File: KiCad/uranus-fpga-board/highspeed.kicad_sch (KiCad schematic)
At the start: 8 parts, among them J1 1040100018, J2 TYPE-C-31-M-12, J4 ASP-134486-01, U6 FT232HL-REEL, U7 93LC56BT, U8 USBLC6-2SC6, U9 W25Q128JVSIQ, Y2 3225-12-20-10-10/4B

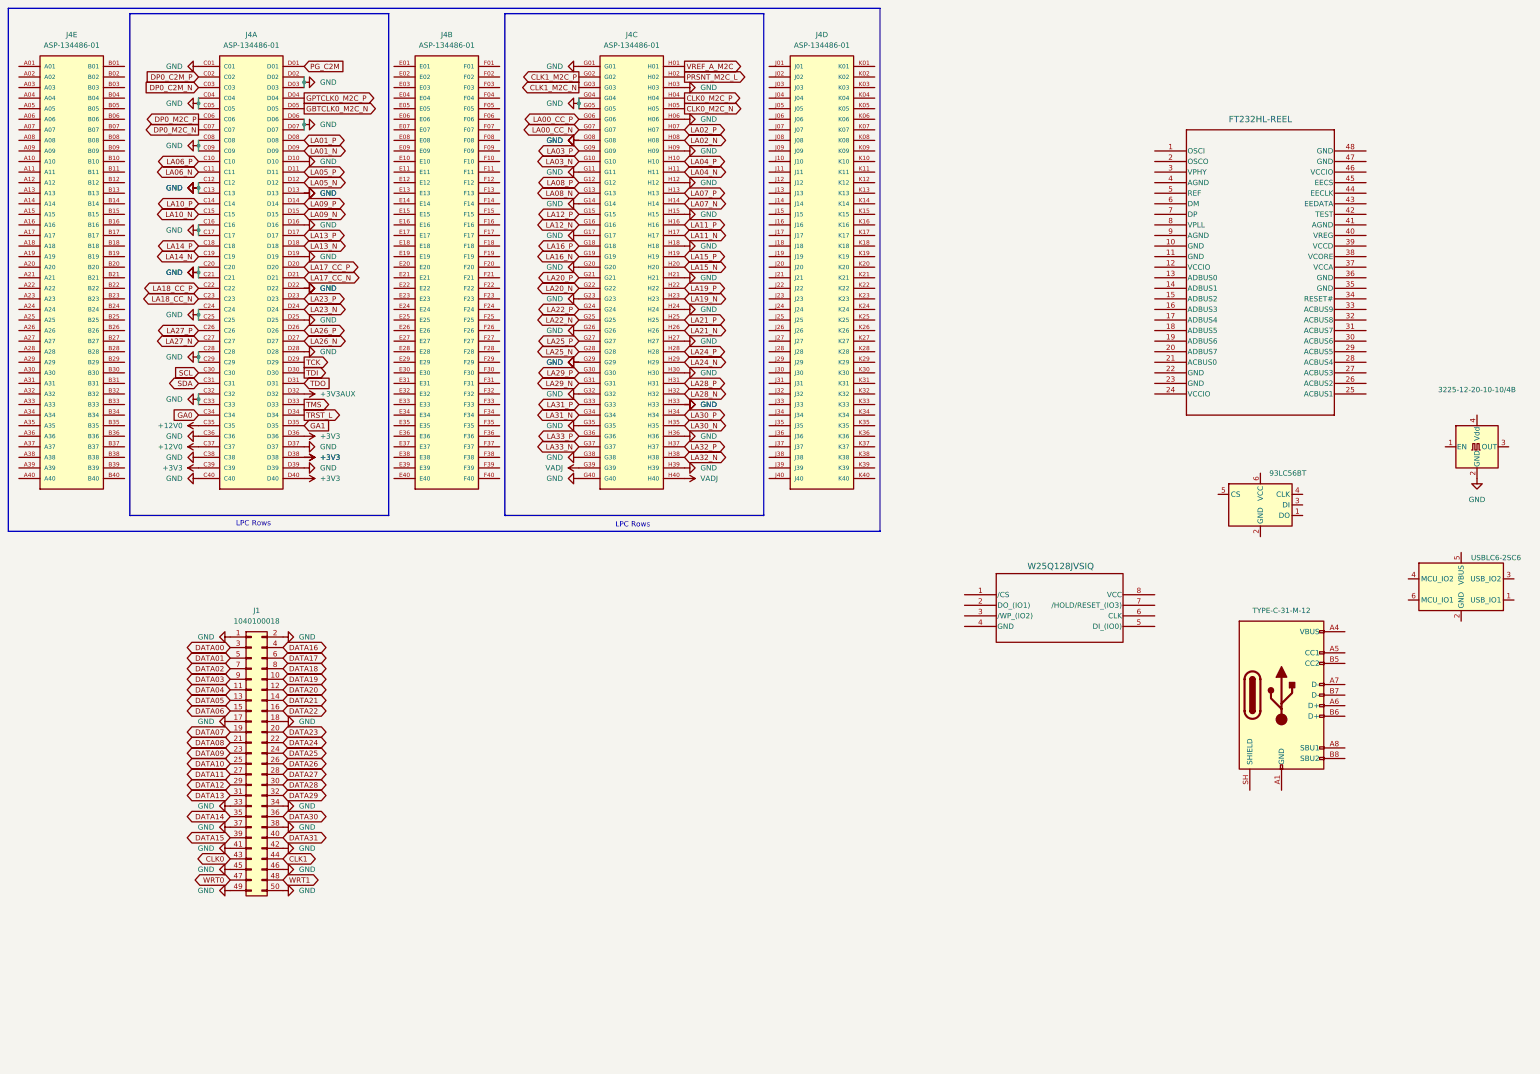
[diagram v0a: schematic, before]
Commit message: New journal, moved BOMS into a new directory
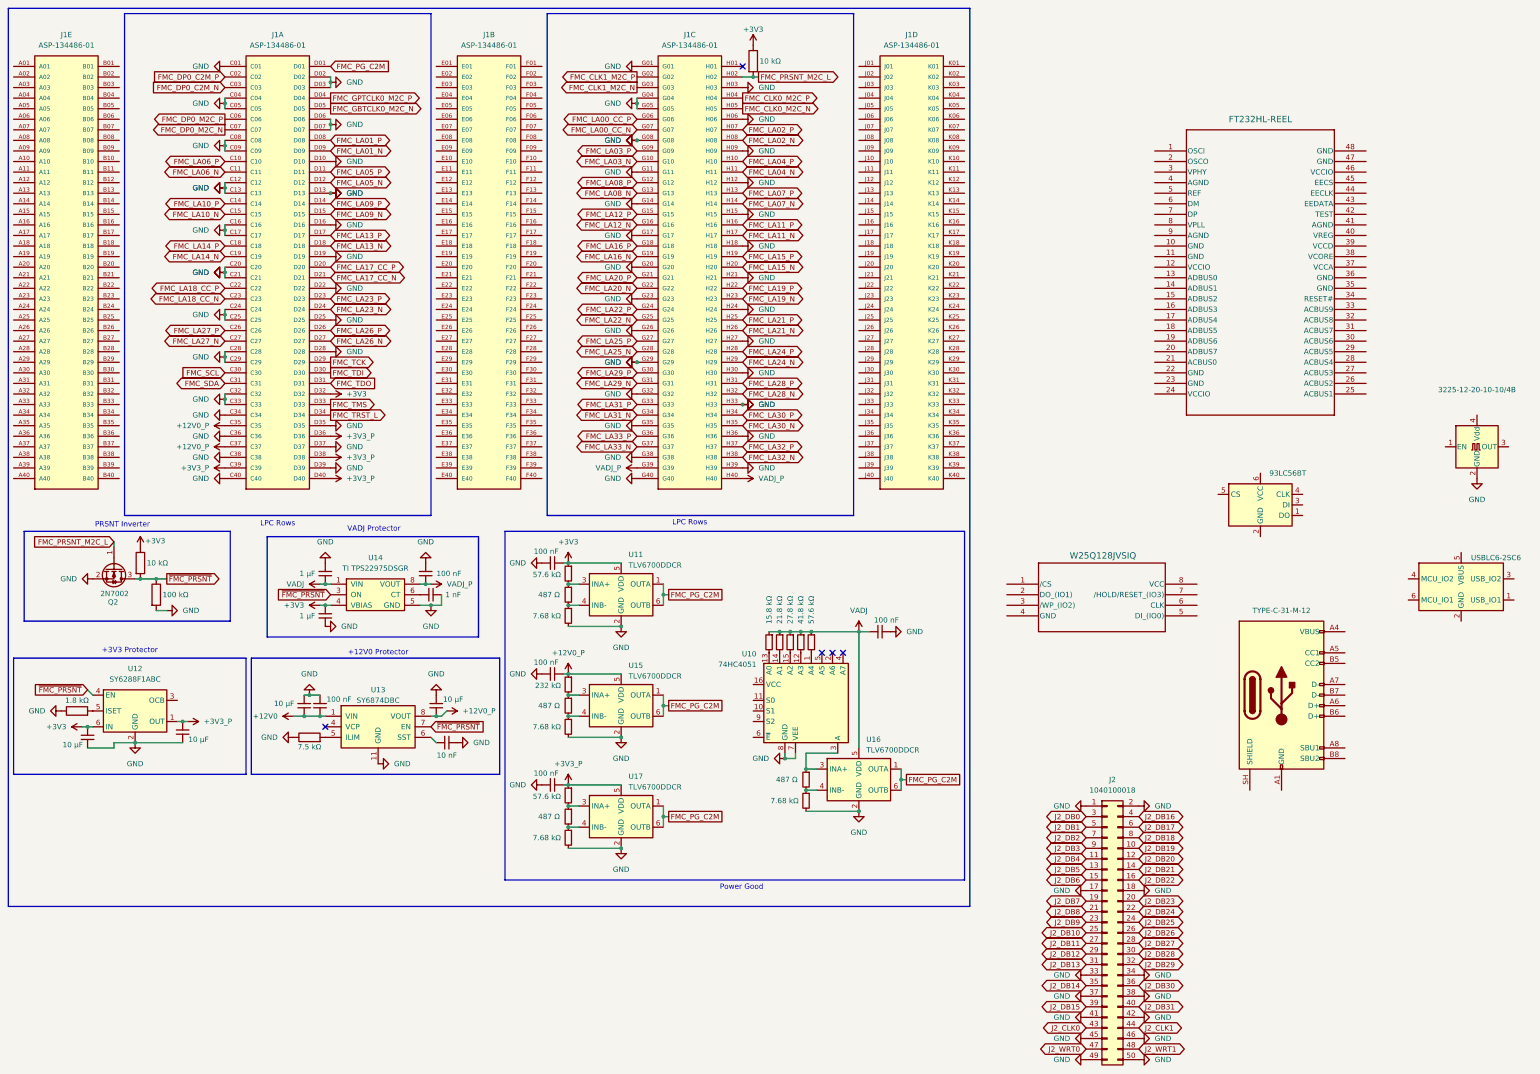
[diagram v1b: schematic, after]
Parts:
- added C68: 1 nF, symbol Device:C_Small
- added C69: 10 nF, symbol Device:C_Small
- added C70, C71, C75, C76: 10 μF, symbol Device:C_Small
- added C72, C77: 1 μF, symbol Device:C_Small
- added C73, C74, C78, C79, C80, C81: 100 nF, symbol Device:C_Small
- added Q2: 2N7002, Package_TO_SOT_SMD:SOT-23, symbol Transistor_FET:2N7002
- added R13, R24, R31: 57.6 kΩ, symbol Device:R_Small
- added R14, R22, R25, R32: 487 Ω, symbol Device:R_Small
- added R15, R16: 10 kΩ, symbol Device:R
- added R17: 7.5 kΩ, symbol Device:R
- added R18: 1.8 kΩ, symbol Device:R
- added R19: 100 kΩ, symbol Device:R
- added R20, R23, R26, R33: 7.68 kΩ, symbol Device:R_Small
- added R21: 232 kΩ, symbol Device:R_Small
- added R27: 41.8 kΩ, symbol Device:R_Small
- added R28: 27.8 kΩ, symbol Device:R_Small
- added R29: 21.8 kΩ, symbol Device:R_Small
- added R30: 15.8 kΩ, symbol Device:R_Small
- added U10: 74HC4051, Package_SO:SOIC-16_3.9x9.9mm_P1.27mm, symbol 74xx:74HC4051
- added U11, U15, U16, U17: TLV6700DDCR, Package_TO_SOT_SMD:SOT-23-6, symbol Sensor_Touch:AT42QT1011-TSHR
- added U12: SY6288F1ABC, Package_TO_SOT_SMD:SOT-23-6, symbol Power_Management:AP2171W
- added U13: SY6874DBC, Package_DFN_QFN:DFN-10-1EP_3x3mm_P0.5mm_EP1.75x2.7mm, symbol Connector_Generic:Conn_02x05_Counter_Clockwise
- added U14: TI TPS22975DSGR, Package_SON:Texas_DSG0008A_WSON-8-1EP_2x2mm_P0.5mm_EP0.9x1.6mm, symbol Connector_Generic:Conn_02x04_Counter_Clockwise
- renumbered J4 to J1, J1 to J2, J2 to J3, U9 to U6, U6 to U7, U7 to U8, U8 to U9
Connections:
- net +3V3AUX is gone; now on net +3V3: J1.D32
- net GA0 is gone; now on net GND: J1.C34
- net GA1 is gone; now on net GND: J1.D35
- net +12V0: now also C74.2, C75.2, U13.1 (VIN), U13.2 (VIN), U13.3 (VIN); no longer J1.C35, J1.C37
- net +3V3: now also C70.1, C77.2, C78.2, R13.1, R15.1, R16.1, U11.5 (VDD), U12.6 (IN), U14.4 (VBIAS); no longer J1.C39, J1.D36, J1.D38, J1.D40
- net GND: now also C68.2, C69.2, C70.2, C71.2, C72.1, C73.1, C74.1, C75.1, C76.1, C77.1, C78.1, C79.1, C80.1, C81.1, Q2.2 (S), R17.1, R18.1, R19.2, R20.2, R23.2, R26.2, R33.2, U10.7 (VEE), U10.8 (GND), U11.2 (GND), U12.2 (GND), U13.11 (GND), U14.5 (GND), U15.2 (GND), U16.2 (GND), U17.2 (GND)
- net VADJ: now also C72.2, C80.2, R24.1, R27.1, R28.1, R29.1, R30.1, U14.1 (VIN), U14.2 (VIN), U16.5 (VDD); no longer J1.G39, J1.H40
- net CLK0 renamed J2_CLK0
- net CLK0_M2C_N renamed FMC_CLK0_M2C_N
- net CLK0_M2C_P renamed FMC_CLK0_M2C_P
- net CLK1 renamed J2_CLK1
- net CLK1_M2C_N renamed FMC_CLK1_M2C_N
- net CLK1_M2C_P renamed FMC_CLK1_M2C_P
- net DATA00 renamed J2_DB0
- net DATA01 renamed J2_DB1
- net DATA02 renamed J2_DB2
- net DATA03 renamed J2_DB3
- net DATA04 renamed J2_DB4
- net DATA05 renamed J2_DB5
- net DATA06 renamed J2_DB6
- net DATA07 renamed J2_DB7
- net DATA08 renamed J2_DB8
- net DATA09 renamed J2_DB9
- net DATA10 renamed J2_DB10
- net DATA11 renamed J2_DB11
- net DATA12 renamed J2_DB12
- net DATA13 renamed J2_DB13
- net DATA14 renamed J2_DB14
- net DATA15 renamed J2_DB15
- net DATA16 renamed J2_DB16
- net DATA17 renamed J2_DB17
- net DATA18 renamed J2_DB18
- net DATA19 renamed J2_DB19
- net DATA20 renamed J2_DB20
- net DATA21 renamed J2_DB21
- net DATA22 renamed J2_DB22
- net DATA23 renamed J2_DB23
- net DATA24 renamed J2_DB24
- net DATA25 renamed J2_DB25
- net DATA26 renamed J2_DB26
- net DATA27 renamed J2_DB27
- net DATA28 renamed J2_DB28
- net DATA29 renamed J2_DB29
- net DATA30 renamed J2_DB30
- net DATA31 renamed J2_DB31
- net DP0_C2M_N renamed FMC_DP0_C2M_N
- net DP0_C2M_P renamed FMC_DP0_C2M_P
- net DP0_M2C_N renamed FMC_DP0_M2C_N
- net DP0_M2C_P renamed FMC_DP0_M2C_P
- net GBTCLK0_M2C_N renamed FMC_GBTCLK0_M2C_N
- net GPTCLK0_M2C_P renamed FMC_GPTCLK0_M2C_P
- net LA00_CC_N renamed FMC_LA00_CC_N
- net LA00_CC_P renamed FMC_LA00_CC_P
- net LA01_N renamed FMC_LA01_N
- net LA01_P renamed FMC_LA01_P
- net LA02_N renamed FMC_LA02_N
- net LA02_P renamed FMC_LA02_P
- net LA03_N renamed FMC_LA03_N
- net LA03_P renamed FMC_LA03_P
- net LA04_N renamed FMC_LA04_N
- net LA04_P renamed FMC_LA04_P
- net LA05_N renamed FMC_LA05_N
- net LA05_P renamed FMC_LA05_P
- net LA06_N renamed FMC_LA06_N
- net LA06_P renamed FMC_LA06_P
- net LA07_N renamed FMC_LA07_N
- net LA07_P renamed FMC_LA07_P
- net LA08_N renamed FMC_LA08_N
- net LA08_P renamed FMC_LA08_P
- net LA09_N renamed FMC_LA09_N
- net LA09_P renamed FMC_LA09_P
- net LA10_N renamed FMC_LA10_N
- net LA10_P renamed FMC_LA10_P
- net LA11_N renamed FMC_LA11_N
- net LA11_P renamed FMC_LA11_P
- net LA12_N renamed FMC_LA12_N
- net LA12_P renamed FMC_LA12_P
- net LA13_N renamed FMC_LA13_N
- net LA13_P renamed FMC_LA13_P
- net LA14_N renamed FMC_LA14_N
- net LA14_P renamed FMC_LA14_P
- net LA15_N renamed FMC_LA15_N
- net LA15_P renamed FMC_LA15_P
- net LA16_N renamed FMC_LA16_N
- net LA16_P renamed FMC_LA16_P
- net LA17_CC_N renamed FMC_LA17_CC_N
- net LA17_CC_P renamed FMC_LA17_CC_P
- net LA18_CC_N renamed FMC_LA18_CC_N
- net LA18_CC_P renamed FMC_LA18_CC_P
- net LA19_N renamed FMC_LA19_N
- net LA19_P renamed FMC_LA19_P
- net LA20_N renamed FMC_LA20_N
- net LA20_P renamed FMC_LA20_P
- net LA21_N renamed FMC_LA21_N
- net LA21_P renamed FMC_LA21_P
- net LA22_N renamed FMC_LA22_N
- net LA22_P renamed FMC_LA22_P
- net LA23_N renamed FMC_LA23_N
- net LA23_P renamed FMC_LA23_P
- net LA24_N renamed FMC_LA24_N
- net LA24_P renamed FMC_LA24_P
- net LA25_N renamed FMC_LA25_N
- net LA25_P renamed FMC_LA25_P
- net LA26_N renamed FMC_LA26_N
- net LA26_P renamed FMC_LA26_P
- net LA27_N renamed FMC_LA27_N
- net LA27_P renamed FMC_LA27_P
- net LA28_N renamed FMC_LA28_N
- net LA28_P renamed FMC_LA28_P
- net LA29_N renamed FMC_LA29_N
- net LA29_P renamed FMC_LA29_P
- net LA30_N renamed FMC_LA30_N
- net LA30_P renamed FMC_LA30_P
- net LA31_N renamed FMC_LA31_N
- net LA31_P renamed FMC_LA31_P
- net LA32_N renamed FMC_LA32_N
- net LA32_P renamed FMC_LA32_P
- net LA33_N renamed FMC_LA33_N
- net LA33_P renamed FMC_LA33_P
- net PG_C2M renamed FMC_PG_C2M
- net FMC_PG_C2M: now also U11.1 (OUTA), U11.6 (OUTB), U15.1 (OUTA), U15.6 (OUTB), U16.1 (OUTA), U16.6 (OUTB), U17.1 (OUTA), U17.6 (OUTB)
- net PRSNT_M2C_L renamed FMC_PRSNT_M2C_L
- net FMC_PRSNT_M2C_L: now also Q2.1 (G), R16.2
- net SCL renamed FMC_SCL
- net SDA renamed FMC_SDA
- net TCK renamed FMC_TCK
- net TDI renamed FMC_TDI
- net TDO renamed FMC_TDO
- net TMS renamed FMC_TMS
- net TRST_L renamed FMC_TRST_L
- net VREF_A_M2C: no longer names the net of J1.H01
- net WRT0 renamed J2_WRT0
- net WRT1 renamed J2_WRT1
- new net: R31.2, R32.1, U17.3 (INA+)
- new net: R17.2, U13.5 (ILIM)
- new net: R13.2, R14.1, U11.3 (INA+)
- new net: R14.2, R20.1, U11.4 (INB-)
- new net: C69.1, U13.6 (SST)
- new net: R22.2, R23.1, U15.4 (INB-)
- new net: R24.2, U10.1 (A4)
- new net: R27.2, U10.12 (A3)
- new net: R30.2, U10.13 (A0)
- new net: R29.2, U10.14 (A1)
- new net: R28.2, U10.15 (A2)
- new net: R25.1, U10.3 (A), U16.3 (INA+)
- new net: R25.2, R26.1, U16.4 (INB-)
- new net: R21.2, R22.1, U15.3 (INA+)
- new net: C68.1, U14.6 (CT)
- new net: R32.2, R33.1, U17.4 (INB-)
- new net: R18.2, U12.5 (ISET)
- new net +12V0_P: C76.2, C79.2, J1.C35, J1.C37, R21.1, U13.10 (VOUT), U13.8 (VOUT), U13.9 (VOUT), U15.5 (VDD)
- new net +3V3_P: C71.1, C81.2, J1.C39, J1.D36, J1.D38, J1.D40, R31.1, U12.1 (OUT), U17.5 (VDD)
- new net VADJ_P: C73.2, J1.G39, J1.H40, U14.7 (VOUT), U14.8 (VOUT)
- new net ~{FMC_PRSNT}: Q2.3 (D), R15.2, R19.1, U12.4 (EN), U13.7 (EN), U14.3 (ON)
- no-connect marks 0 -> 5
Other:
- note added: "+12V0 Protector"
- note added: "+3V3 Protector"
- note added: "PRSNT Inverter"
- note added: "Power Good"
- note added: "VADJ Protector"
- moved on the sheet: J1A, J1B, J1C, J1D, J1E, J2

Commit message: Oct 18 journal
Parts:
- removed C80: 100 nF, symbol Device:C_Small
- removed R24: 57.6 kΩ, symbol Device:R_Small
- removed R27: 41.8 kΩ, symbol Device:R_Small
- removed R28: 27.8 kΩ, symbol Device:R_Small
- removed R29: 21.8 kΩ, symbol Device:R_Small
- removed R30: 15.8 kΩ, symbol Device:R_Small
- removed U10: 74HC4051, Package_SO:SOIC-16_3.9x9.9mm_P1.27mm, symbol 74xx:74HC4051
- added C68, C85, C86, C87, C88, C89, C90: 100 nF, symbol Device:C_Small
- added C79, C81, C83, C91: 10 nF, symbol Device:C_Small
- added C92: 1 nF, symbol Device:C_Small
- added R16, R36, R37, R39: 200 kΩ, Resistor_SMD:R_0402_1005Metric, symbol Device:R_Small
- added R18: 10 kΩ, symbol Device:R
- added R31: 15.8 kΩ, Resistor_SMD:R_0402_1005Metric, symbol Device:R_Small
- added R32: 21.5 kΩ, Resistor_SMD:R_0402_1005Metric, symbol Device:R_Small
- added R33: 27.4 kΩ, Resistor_SMD:R_0402_1005Metric, symbol Device:R_Small
- added R34: 41.2 kΩ, Resistor_SMD:R_0402_1005Metric, symbol Device:R_Small
- added R35: 57.6 kΩ, Resistor_SMD:R_0402_1005Metric, symbol Device:R_Small
- added U13: TMUX1108PW, Package_SO:TSSOP-16_4.4x5mm_P0.65mm, symbol Analog_Switch:TMUX1108PW
- added U6: TPS2553DBVR, Package_TO_SOT_SMD:SOT-23-6, symbol Battery_Management:BQ21040DBV
- C80: renamed from C78; value 100 nF -> 1 nF
- C82: renamed from C79; value 100 nF -> 1 nF
- C84: renamed from C81; value 100 nF -> 1 nF
- R19: renamed from R13; footprint (none) -> Resistor_SMD:R_0402_1005Metric
- R20: renamed from R14; value 487 Ω -> 499 Ω; footprint (none) -> Resistor_SMD:R_0201_0603Metric
- R21: renamed from R20; footprint (none) -> Resistor_SMD:R_0402_1005Metric
- R22: renamed from R21; footprint (none) -> Resistor_SMD:R_0402_1005Metric
- R23: renamed from R22; value 487 Ω -> 499 Ω; footprint (none) -> Resistor_SMD:R_0201_0603Metric
- R24: renamed from R23; footprint (none) -> Resistor_SMD:R_0402_1005Metric
- R25: renamed from R31; footprint (none) -> Resistor_SMD:R_0402_1005Metric
- R26: renamed from R32; value 487 Ω -> 499 Ω; footprint (none) -> Resistor_SMD:R_0201_0603Metric
- R27: renamed from R33; footprint (none) -> Resistor_SMD:R_0402_1005Metric
- R29: renamed from R25; value 487 Ω -> 499 Ω; footprint (none) -> Resistor_SMD:R_0201_0603Metric
- R30: renamed from R26; footprint (none) -> Resistor_SMD:R_0402_1005Metric
- renumbered C70 to C69, C71 to C70, C75 to C71, C74 to C72, C72 to C73, C77 to C74, C73 to C75, C68 to C76, C76 to C77, C69 to C78, Q2 to Q1, R18 to R13, R15 to R14, R19 to R15, R16 to R28, U11 to U10, U15 to U11, U17 to U12, U16 to U14, U6 to U15, U7 to U16, U8 to U17, U9 to U18, U12 to U7, U13 to U8, U14 to U9
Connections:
- net +12V0_P: now also C81.2; no longer U11.5 (VDD)
- net +3V3: now also U11.5 (VDD), U12.5 (VDD), U14.5 (VDD), C68.2, C85.2, C86.2, C87.2, C90.2, U6.4 (EN), U6.6 (IN); no longer C80.2, J1.D32, R19.1
- net +3V3_P: now also C83.2, R18.1; no longer U12.5 (VDD)
- net FMC_PG_C2M: now also R18.2
- net GND: now also C68.1, C79.1, C81.1, C83.1, C85.1, C86.1, C87.1, C88.1, C88.2, C89.1, C90.1, C91.1, C92.1, R16.2, R36.2, R37.1, R39.1, U13.14 (GND), U13.3 (VSS), U6.5 (GND)
- net VADJ: no longer U14.5 (VDD)
- net VADJ_P: now also C91.2, C92.2, R31.1, R32.1, R33.1, R34.1, R35.1
- net at R29.1, U14.3 (INA+): now also U13.8 (D)
- new net: R16.1, U6.3 (ILIM)
- new net: R35.2, U13.11 (S6)
- new net: R32.2, U13.6 (S3)
- new net: R31.2, U13.5 (S2)
- new net: R34.2, U13.12 (S5)
- new net: R33.2, U13.7 (S4)
- new net +3V3AUX: C79.2, C80.2, J1.D32, R19.1, U6.2 (OUT)
- new net +5V0: C89.2, U13.13 (VDD), U13.2 (EN)
- new net VADJ_VSW_A0: R36.1, U13.1 (A0)
- new net VADJ_VSW_A1: R37.2, U13.16 (A1)
- new net VADJ_VSW_A2: R39.2, U13.15 (A2)
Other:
- note added: "+1V2"
- note added: "+1V5"
- note added: "+1V8"
- note added: "+2V5"
- note added: "+3V3"
- note added: "+3V3AUX Protector"
- note added: "opt."
- moved on the sheet: Q1, U11, U12, U14, U7, U8
